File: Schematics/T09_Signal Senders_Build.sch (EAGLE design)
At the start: 34 parts, among them IC1 7805TV, IC2 ATMEGA328, IC3 7805TV, SW1 , Y2 16MHz

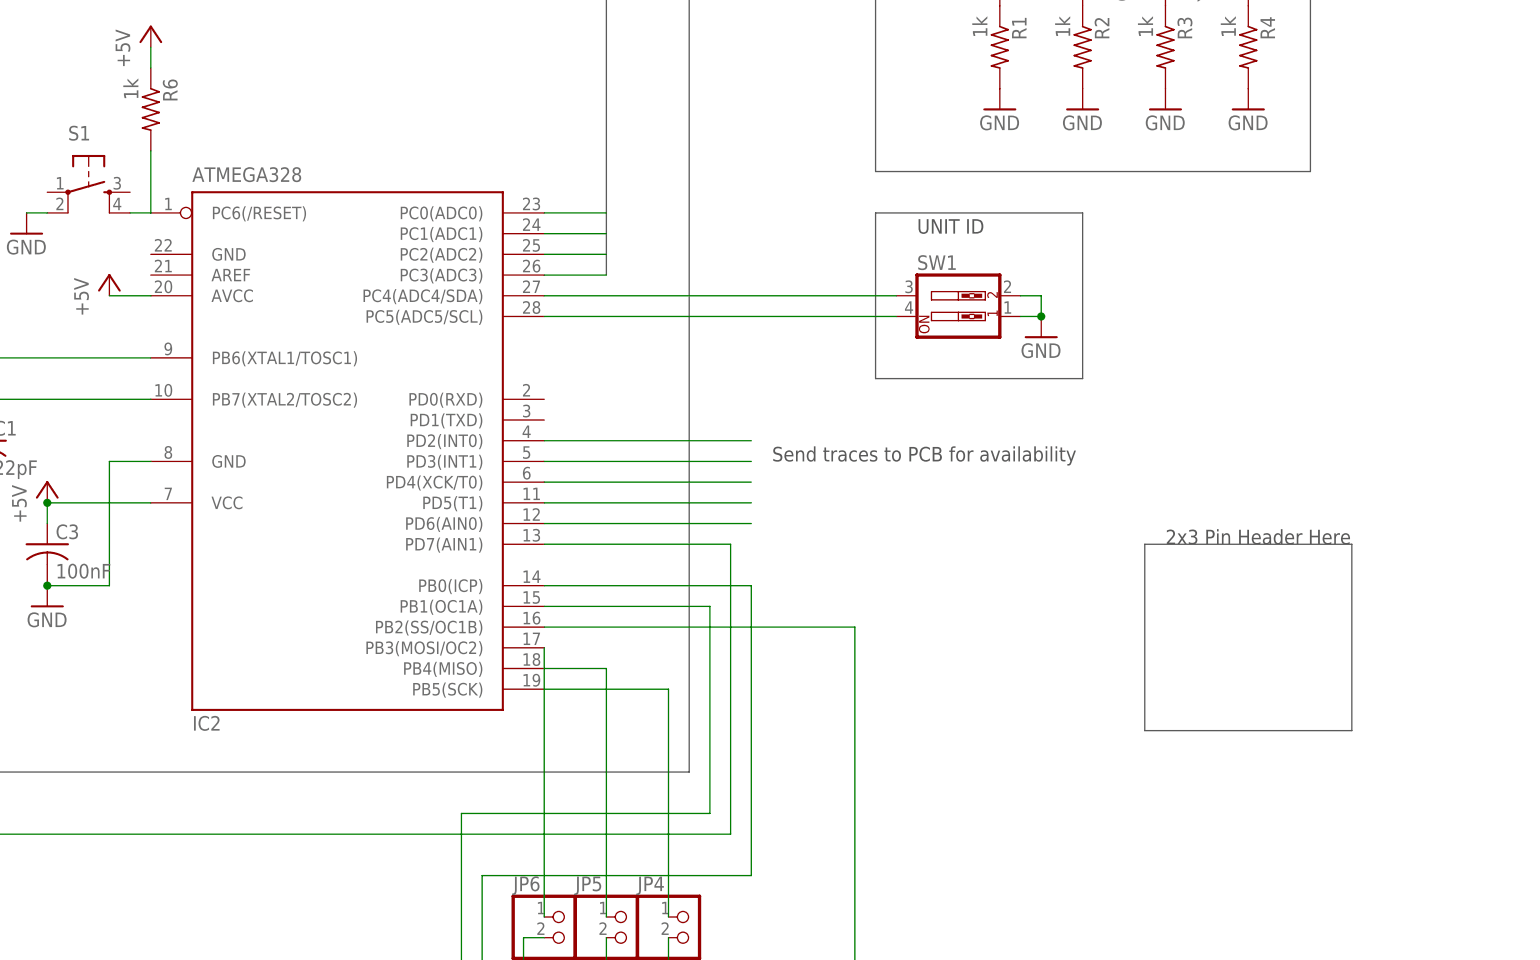
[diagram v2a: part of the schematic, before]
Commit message: add 6 pin header for programming
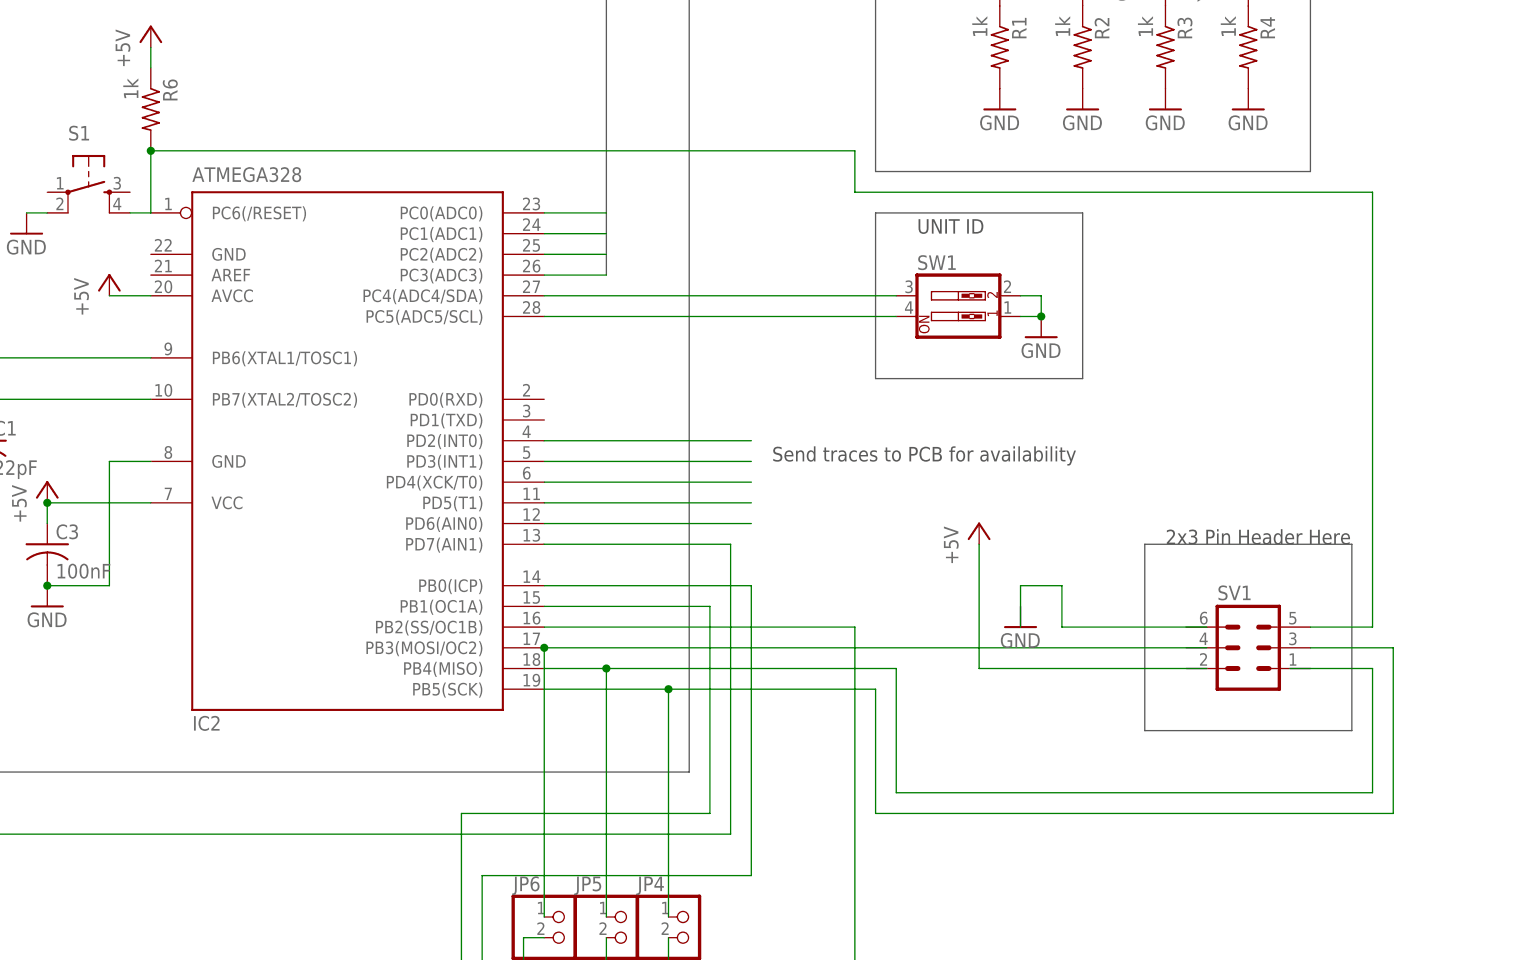
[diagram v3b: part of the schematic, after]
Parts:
- added SV1: (no value), con-lstb:MA03-2
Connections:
- net N$1: now also SV1.5
- net RF_SPI5: now also SV1.3
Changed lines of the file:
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@@
 <?xml version="1.0" encoding="utf-8"?>
 <!DOCTYPE eagle SYSTEM "eagle.dtd">
-<eagle version="6.3">
+<eagle version="6.5.0">
 <drawing>
 <settings>
@@
 <part name="X1" library="con-conrad" deviceset="73398?" device="0-62"/>
 <part name="JP3" library="pinhead" deviceset="PINHD-1X2" device="/90"/>
+<part name="SV1" library="con-lstb" deviceset="MA03-2" device=""/>
+<part name="P+7" library="supply1" deviceset="+5V" device=""/>
+<part name="GND16" library="supply1" deviceset="GND" device=""/>
 </parts>
 <sheets>
@@
 <instance part="X1" gate="G$1" x="35.56" y="233.68" rot="MR0"/>
 <instance part="JP3" gate="G$1" x="53.34" y="208.28" rot="R270"/>
+<instance part="SV1" gate="1" x="322.58" y="96.52"/>
+<instance part="P+7" gate="1" x="289.56" y="111.76"/>
+<instance part="GND16" gate="1" x="294.64" y="99.06"/>
 </instances>
 <busses>
@@
 <pinref part="R6" gate="G$1" pin="1"/>
 <wire x1="187.96" y1="170.18" x2="187.96" y2="167.64" width="0.1524" layer="91"/>
+</segment>
+<segment>
+<wire x1="317.5" y1="93.98" x2="289.56" y2="93.98" width="0.1524" layer="91"/>
+<pinref part="P+7" gate="1" pin="+5V"/>
+<wire x1="289.56" y1="93.98" x2="289.56" y2="109.22" width="0.1524" layer="91"/>
 </segment>
 </net>
@@
 <pinref part="R6" gate="G$1" pin="2"/>
 <wire x1="187.96" y1="157.48" x2="187.96" y2="149.86" width="0.1524" layer="91"/>
+<wire x1="187.96" y1="157.48" x2="274.32" y2="157.48" width="0.1524" layer="91"/>
+<wire x1="274.32" y1="157.48" x2="274.32" y2="152.4" width="0.1524" layer="91"/>
+<junction x="187.96" y="157.48"/>
+<wire x1="274.32" y1="152.4" x2="337.82" y2="152.4" width="0.1524" layer="91"/>
+<wire x1="337.82" y1="152.4" x2="337.82" y2="99.06" width="0.1524" layer="91"/>
+<pinref part="SV1" gate="1" pin="5"/>
+<wire x1="337.82" y1="99.06" x2="330.2" y2="99.06" width="0.1524" layer="91"/>
 </segment>
 </net>
@@
 <pinref part="JP6" gate="G$1" pin="1"/>
 <wire x1="236.22" y1="96.52" x2="236.22" y2="63.5" width="0.1524" layer="91"/>
+<wire x1="236.22" y1="96.52" x2="317.5" y2="96.52" width="0.1524" layer="91"/>
+<junction x="236.22" y="96.52"/>
 </segment>
 <segment>
@@
 <wire x1="236.22" y1="93.98" x2="243.84" y2="93.98" width="0.1524" layer="91"/>
 <wire x1="243.84" y1="93.98" x2="243.84" y2="63.5" width="0.1524" layer="91"/>
+<wire x1="243.84" y1="93.98" x2="279.4" y2="93.98" width="0.1524" layer="91"/>
+<junction x="243.84" y="93.98"/>
+<wire x1="279.4" y1="93.98" x2="279.4" y2="78.74" width="0.1524" layer="91"/>
+<wire x1="279.4" y1="78.74" x2="337.82" y2="78.74" width="0.1524" layer="91"/>
+<wire x1="337.82" y1="93.98" x2="327.66" y2="93.98" width="0.1524" layer="91"/>
+<wire x1="337.82" y1="93.98" x2="337.82" y2="78.74" width="0.1524" layer="91"/>
 </segment>
 <segment>
@@
 <pinref part="JP4" gate="G$1" pin="1"/>
 <wire x1="251.46" y1="63.5" x2="251.46" y2="91.44" width="0.1524" layer="91"/>
+<wire x1="251.46" y1="91.44" x2="276.86" y2="91.44" width="0.1524" layer="91"/>
+<junction x="251.46" y="91.44"/>
+<wire x1="276.86" y1="91.44" x2="276.86" y2="76.2" width="0.1524" layer="91"/>
+<wire x1="276.86" y1="76.2" x2="340.36" y2="76.2" width="0.1524" layer="91"/>
+<wire x1="340.36" y1="76.2" x2="340.36" y2="96.52" width="0.1524" layer="91"/>
+<pinref part="SV1" gate="1" pin="3"/>
+<wire x1="340.36" y1="96.52" x2="330.2" y2="96.52" width="0.1524" layer="91"/>
 </segment>
 </net>
@@
 </segment>
 </net>
+<net name="N$19" class="0">
+<segment>
+<wire x1="317.5" y1="99.06" x2="299.72" y2="99.06" width="0.1524" layer="91"/>
+<wire x1="299.72" y1="99.06" x2="299.72" y2="104.14" width="0.1524" layer="91"/>
+<wire x1="299.72" y1="104.14" x2="294.64" y2="104.14" width="0.1524" layer="91"/>
+<wire x1="294.64" y1="104.14" x2="294.64" y2="99.06" width="0.1524" layer="91"/>
+</segment>
+</net>

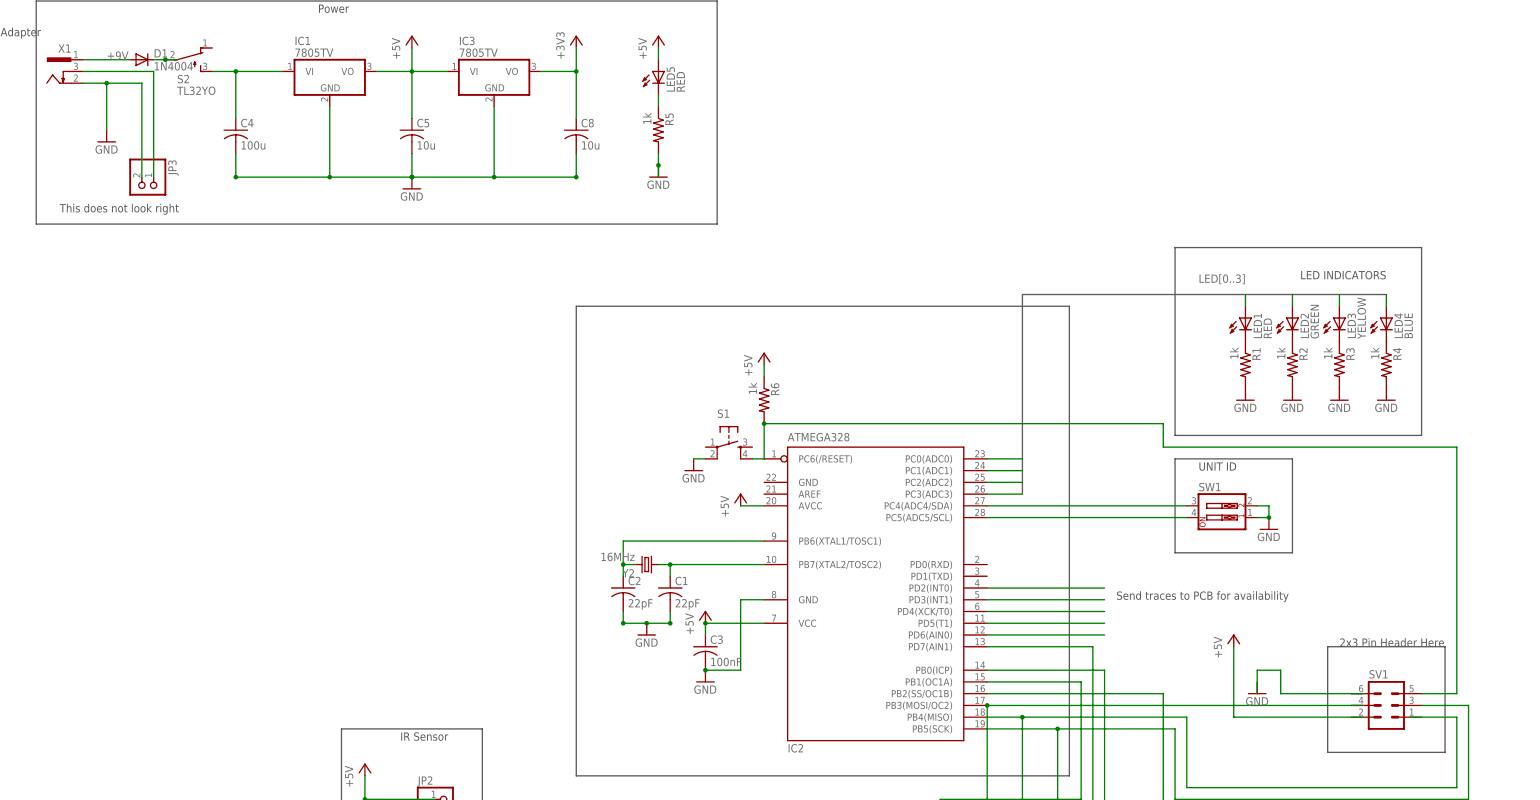
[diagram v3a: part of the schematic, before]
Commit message: Fixed many ERC errors
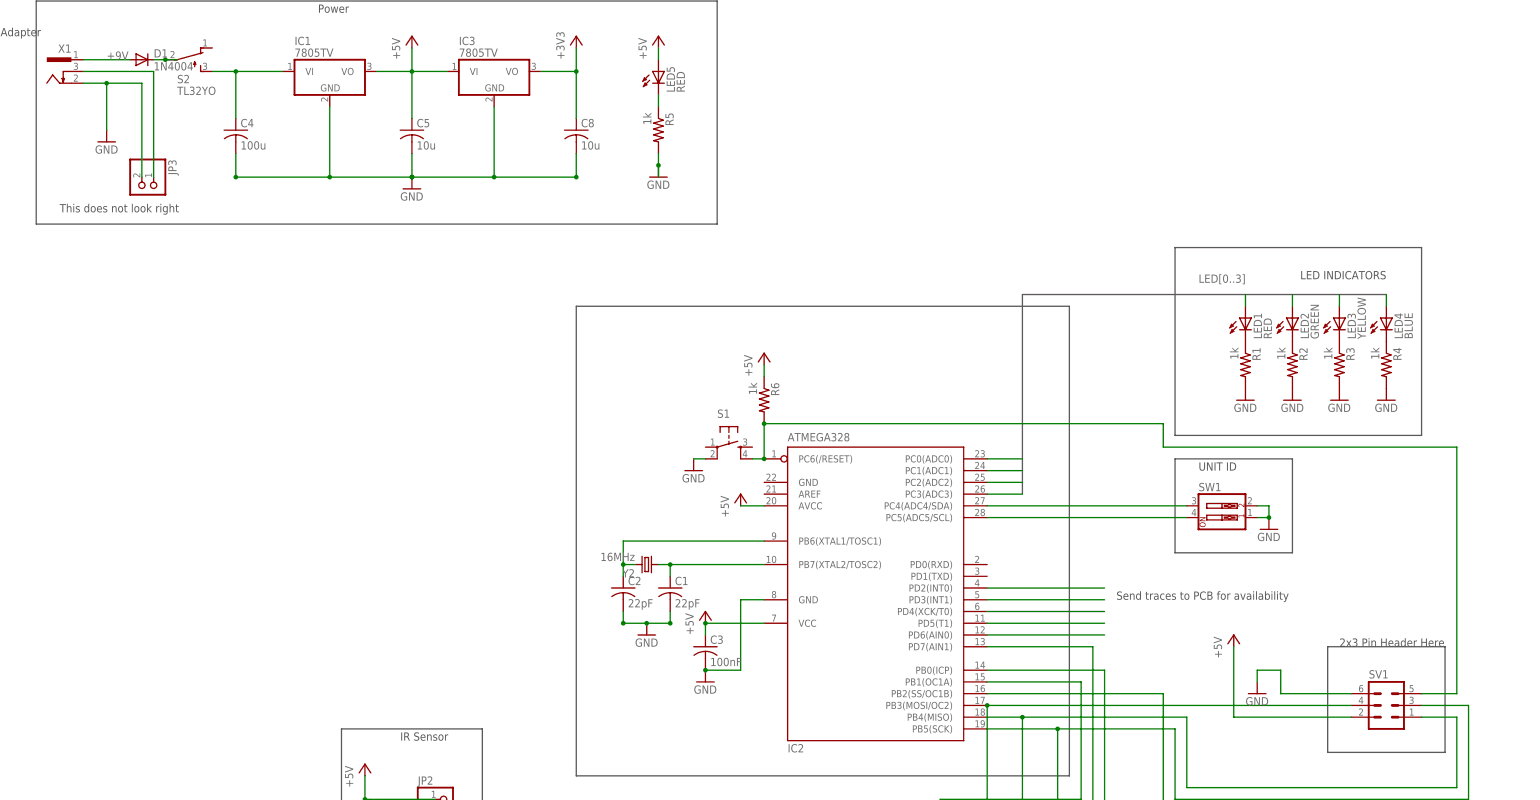
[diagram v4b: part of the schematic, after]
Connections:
- net +5V: now also SV1.2
- net GND: now also JP3.2, SV1.6, X1.2
- net N$13: now also JP3.1
- net RF_SPI3: now also SV1.4
- net RF_SPI4: now also SV1.1
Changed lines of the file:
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@@
 </segment>
 <segment>
-<wire x1="317.5" y1="93.98" x2="289.56" y2="93.98" width="0.1524" layer="91"/>
 <pinref part="P+7" gate="1" pin="+5V"/>
 <wire x1="289.56" y1="93.98" x2="289.56" y2="109.22" width="0.1524" layer="91"/>
+<pinref part="SV1" gate="1" pin="2"/>
+<wire x1="314.96" y1="93.98" x2="289.56" y2="93.98" width="0.1524" layer="91"/>
 </segment>
 </net>
@@
 <pinref part="GND13" gate="1" pin="GND"/>
 <wire x1="45.72" y1="220.98" x2="45.72" y2="231.14" width="0.1524" layer="91"/>
-<wire x1="45.72" y1="231.14" x2="40.64" y2="231.14" width="0.1524" layer="91"/>
+<wire x1="53.34" y1="231.14" x2="45.72" y2="231.14" width="0.1524" layer="91"/>
+<pinref part="JP3" gate="G$1" pin="2"/>
+<wire x1="53.34" y1="210.82" x2="53.34" y2="231.14" width="0.1524" layer="91"/>
+<pinref part="X1" gate="G$1" pin="2"/>
+<wire x1="40.64" y1="231.14" x2="45.72" y2="231.14" width="0.1524" layer="91"/>
 <junction x="45.72" y="231.14"/>
-<wire x1="53.34" y1="210.82" x2="53.34" y2="231.14" width="0.1524" layer="91"/>
-<wire x1="53.34" y1="231.14" x2="45.72" y2="231.14" width="0.1524" layer="91"/>
 </segment>
 <segment>
@@
 <pinref part="GND15" gate="1" pin="GND"/>
 <wire x1="101.6" y1="68.58" x2="101.6" y2="66.04" width="0.1524" layer="91"/>
+</segment>
+<segment>
+<wire x1="299.72" y1="99.06" x2="299.72" y2="104.14" width="0.1524" layer="91"/>
+<wire x1="299.72" y1="104.14" x2="294.64" y2="104.14" width="0.1524" layer="91"/>
+<pinref part="GND16" gate="1" pin="GND"/>
+<wire x1="294.64" y1="104.14" x2="294.64" y2="101.6" width="0.1524" layer="91"/>
+<pinref part="SV1" gate="1" pin="6"/>
+<wire x1="299.72" y1="99.06" x2="314.96" y2="99.06" width="0.1524" layer="91"/>
 </segment>
 </net>
@@
 <pinref part="SV1" gate="1" pin="5"/>
 <wire x1="337.82" y1="99.06" x2="330.2" y2="99.06" width="0.1524" layer="91"/>
+<junction x="187.96" y="149.86"/>
 </segment>
 </net>
@@
 <pinref part="JP6" gate="G$1" pin="1"/>
 <wire x1="236.22" y1="96.52" x2="236.22" y2="63.5" width="0.1524" layer="91"/>
-<wire x1="236.22" y1="96.52" x2="317.5" y2="96.52" width="0.1524" layer="91"/>
+<pinref part="SV1" gate="1" pin="4"/>
+<wire x1="236.22" y1="96.52" x2="314.96" y2="96.52" width="0.1524" layer="91"/>
 <junction x="236.22" y="96.52"/>
 </segment>
@@
 <wire x1="279.4" y1="93.98" x2="279.4" y2="78.74" width="0.1524" layer="91"/>
 <wire x1="279.4" y1="78.74" x2="337.82" y2="78.74" width="0.1524" layer="91"/>
-<wire x1="337.82" y1="93.98" x2="327.66" y2="93.98" width="0.1524" layer="91"/>
 <wire x1="337.82" y1="93.98" x2="337.82" y2="78.74" width="0.1524" layer="91"/>
+<pinref part="SV1" gate="1" pin="1"/>
+<wire x1="337.82" y1="93.98" x2="330.2" y2="93.98" width="0.1524" layer="91"/>
 </segment>
 <segment>
@@
 <pinref part="X1" gate="G$1" pin="3"/>
 <wire x1="40.64" y1="233.68" x2="55.88" y2="233.68" width="0.1524" layer="91"/>
+<pinref part="JP3" gate="G$1" pin="1"/>
 <wire x1="55.88" y1="233.68" x2="55.88" y2="210.82" width="0.1524" layer="91"/>
 </segment>
 </net>
-<net name="N$19" class="0">
-<segment>
-<wire x1="317.5" y1="99.06" x2="299.72" y2="99.06" width="0.1524" layer="91"/>
-<wire x1="299.72" y1="99.06" x2="299.72" y2="104.14" width="0.1524" layer="91"/>
-<wire x1="299.72" y1="104.14" x2="294.64" y2="104.14" width="0.1524" layer="91"/>
-<wire x1="294.64" y1="104.14" x2="294.64" y2="99.06" width="0.1524" layer="91"/>
-</segment>
-</net>
